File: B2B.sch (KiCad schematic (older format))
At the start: 3 parts, among them P4 CONN_01X14, P5 CONN_01X07, P6 CONN_01X07

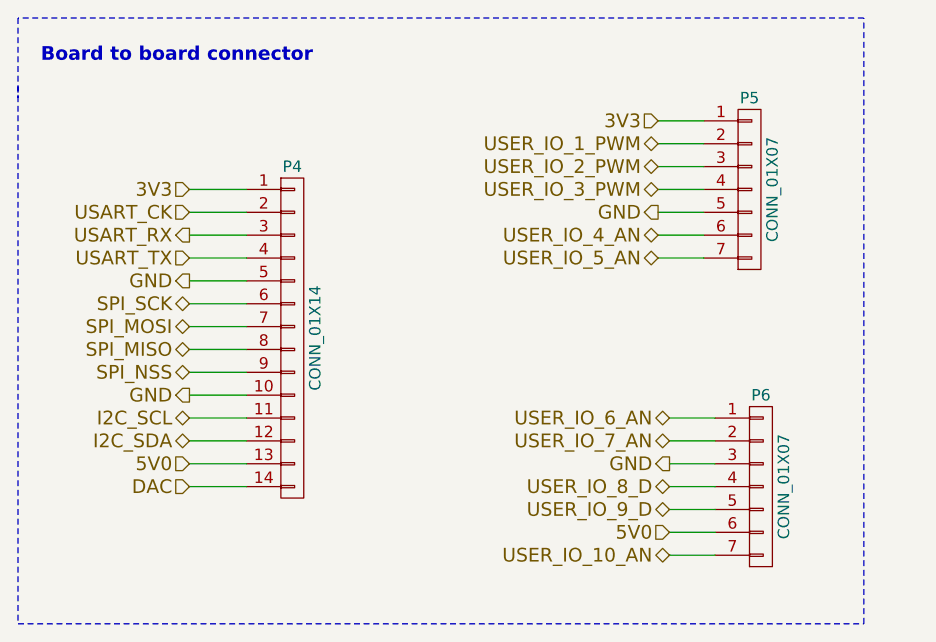
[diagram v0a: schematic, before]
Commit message: - #4 Added UART and CAN interface transceivers - Improved schematic structure - Removed all gerber outputs - Generated schematics outputs for PCB design - Updated local libraries
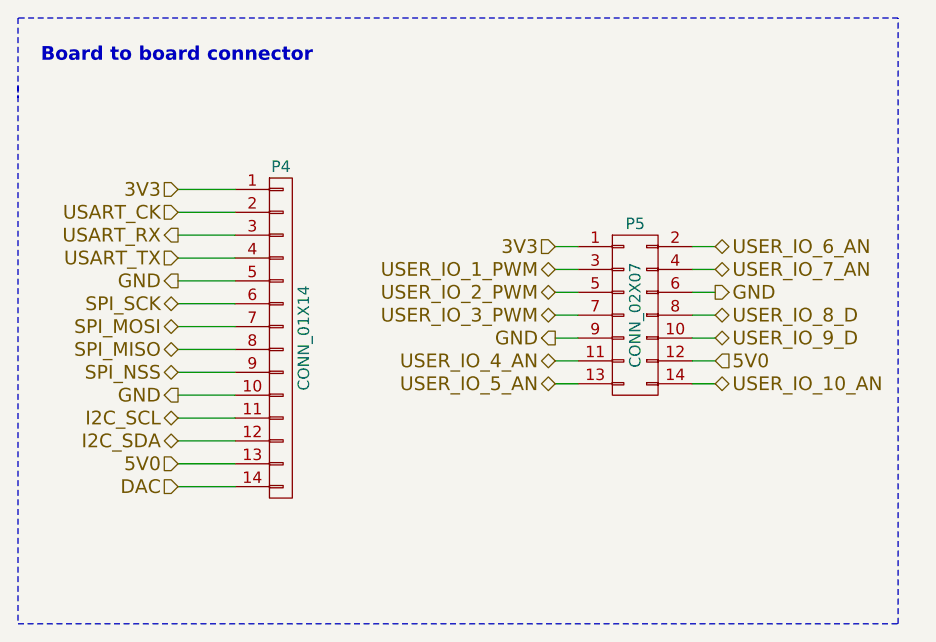
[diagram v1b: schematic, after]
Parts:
- removed P5, P6: CONN_01X07, symbol CONN_01X07
- added P5: CONN_02X07, Pin_Headers:Pin_Header_Straight_2x07, symbol CONN_02X07
- P4: footprint (none) -> Pin_Headers:Pin_Header_Straight_1x14
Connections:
- net 3V3: now also P5.1 (P1)
- net 5V0: now also P5.12 (P12)
- net GND: now also P5.6 (P6), P5.9 (P9)
- net USER_IO_10_AN: now also P5.14 (P14)
- net USER_IO_1_PWM: now also P5.3 (P3)
- net USER_IO_2_PWM: now also P5.5 (P5)
- net USER_IO_3_PWM: now also P5.7 (P7)
- net USER_IO_4_AN: now also P5.11 (P11)
- net USER_IO_5_AN: now also P5.13 (P13)
- net USER_IO_6_AN: now also P5.2 (P2)
- net USER_IO_7_AN: now also P5.4 (P4)
- net USER_IO_8_D: now also P5.8 (P8)
- net USER_IO_9_D: now also P5.10 (P10)
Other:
- moved on the sheet: P4
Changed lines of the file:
@@
 L CONN_01X14 P4
 U 1 1 56104092
-P 5350 4100
-F 0 "P4" H 5350 4850 50  0000 C CNN
-F 1 "CONN_01X14" V 5450 4100 50  0000 C CNN
-F 2 "" H 5350 4100 60  0000 C CNN
-F 3 "" H 5350 4100 60  0000 C CNN
-	1    5350 4100
+P 5300 4100
+F 0 "P4" H 5300 4850 50  0000 C CNN
+F 1 "CONN_01X14" V 5400 4100 50  0000 C CNN
+F 2 "Pin_Headers:Pin_Header_Straight_1x14" H 5300 4100 60  0001 C CNN
+F 3 "" H 5300 4100 60  0000 C CNN
+	1    5300 4100
 	1    0    0    -1
 $EndComp
-Text HLabel 4900 3450 0    60   Input ~ 0
+Text HLabel 4850 3450 0    60   Input ~ 0
 3V3
 Wire Wire Line
-	4900 3450 5150 3450
+	4850 3450 5100 3450
 Wire Wire Line
-	4900 3550 5150 3550
+	4850 3550 5100 3550
 Wire Wire Line
-	4900 3650 5150 3650
+	4850 3650 5100 3650
 Wire Wire Line
-	4900 3750 5150 3750
+	4850 3750 5100 3750
 Wire Wire Line
-	4900 3850 5150 3850
+	4850 3850 5100 3850
 Wire Wire Line
-	4900 3950 5150 3950
+	4850 3950 5100 3950
 Wire Wire Line
-	4900 4050 5150 4050
+	4850 4050 5100 4050
 Wire Wire Line
-	4900 4150 5150 4150
+	4850 4150 5100 4150
 Wire Wire Line
-	4900 4250 5150 4250
+	4850 4250 5100 4250
 Wire Wire Line
-	4900 4350 5150 4350
+	4850 4350 5100 4350
 Wire Wire Line
-	4900 4450 5150 4450
+	4850 4450 5100 4450
 Wire Wire Line
-	4900 4550 5150 4550
+	4850 4550 5100 4550
 Wire Wire Line
-	4900 4650 5150 4650
+	4850 4650 5100 4650
 Wire Wire Line
-	4900 4750 5150 4750
-Wire Wire Line
-	6950 3150 7150 3150
-Wire Wire Line
-	6950 3250 7150 3250
-Wire Wire Line
-	6950 3350 7150 3350
-Wire Wire Line
-	6950 3450 7150 3450
-Wire Wire Line
-	6950 3550 7150 3550
-Wire Wire Line
-	6950 3650 7150 3650
-Wire Wire Line
-	6950 3750 7150 3750
-Wire Wire Line
-	7000 4450 7200 4450
-Wire Wire Line
-	7000 4550 7200 4550
-Wire Wire Line
-	7000 4650 7200 4650
-Wire Wire Line
-	7000 4750 7200 4750
-Wire Wire Line
-	7000 4850 7200 4850
-Wire Wire Line
-	7000 4950 7200 4950
-Wire Wire Line
-	7000 5050 7200 5050
-Text HLabel 6950 3150 0    60   Input ~ 0
+	4850 4750 5100 4750
+Text HLabel 6500 3700 0    60   Input ~ 0
 3V3
-Text HLabel 6950 3550 0    60   Output ~ 0
+Text HLabel 6500 4100 0    60   Output ~ 0
 GND
-Text HLabel 7000 4650 0    60   Output ~ 0
+Text HLabel 7200 3900 2    60   Output ~ 0
 GND
-Text HLabel 4900 3850 0    60   Output ~ 0
+Text HLabel 4850 3850 0    60   Output ~ 0
 GND
-Text HLabel 4900 4350 0    60   Output ~ 0
+Text HLabel 4850 4350 0    60   Output ~ 0
 GND
-Text HLabel 7000 4950 0    60   Input ~ 0
+Text HLabel 7200 4200 2    60   Input ~ 0
 5V0
-Text HLabel 4900 4650 0    60   Input ~ 0
+Text HLabel 4850 4650 0    60   Input ~ 0
 5V0
-Text HLabel 4900 3550 0    60   Input ~ 0
+Text HLabel 4850 3550 0    60   Input ~ 0
 USART_CK
-Text HLabel 4900 3650 0    60   Output ~ 0
+Text HLabel 4850 3650 0    60   Output ~ 0
 USART_RX
-Text HLabel 4900 3750 0    60   Input ~ 0
+Text HLabel 4850 3750 0    60   Input ~ 0
 USART_TX
-Text HLabel 4900 3950 0    60   BiDi ~ 0
+Text HLabel 4850 3950 0    60   BiDi ~ 0
 SPI_SCK
-Text HLabel 4900 4050 0    60   BiDi ~ 0
+Text HLabel 4850 4050 0    60   BiDi ~ 0
 SPI_MOSI
-Text HLabel 4900 4150 0    60   BiDi ~ 0
+Text HLabel 4850 4150 0    60   BiDi ~ 0
 SPI_MISO
-Text HLabel 4900 4250 0    60   BiDi ~ 0
+Text HLabel 4850 4250 0    60   BiDi ~ 0
 SPI_NSS
-Text HLabel 4900 4450 0    60   BiDi ~ 0
+Text HLabel 4850 4450 0    60   BiDi ~ 0
 I2C_SCL
-Text HLabel 4900 4550 0    60   BiDi ~ 0
+Text HLabel 4850 4550 0    60   BiDi ~ 0
 I2C_SDA
-Text HLabel 4900 4750 0    60   Input ~ 0
+Text HLabel 4850 4750 0    60   Input ~ 0
 DAC
-Text HLabel 6950 3250 0    60   BiDi ~ 0
+Text HLabel 6500 3800 0    60   BiDi ~ 0
 USER_IO_1_PWM
-Text HLabel 6950 3350 0    60   BiDi ~ 0
+Text HLabel 6500 3900 0    60   BiDi ~ 0
 USER_IO_2_PWM
-Text HLabel 6950 3450 0    60   BiDi ~ 0
+Text HLabel 6500 4000 0    60   BiDi ~ 0
 USER_IO_3_PWM
-Text HLabel 6950 3650 0    60   BiDi ~ 0
+Text HLabel 6500 4200 0    60   BiDi ~ 0
 USER_IO_4_AN
-Text HLabel 6950 3750 0    60   BiDi ~ 0
+Text HLabel 6500 4300 0    60   BiDi ~ 0
 USER_IO_5_AN
-Text HLabel 7000 4450 0    60   BiDi ~ 0
+Text HLabel 7200 3700 2    60   BiDi ~ 0
 USER_IO_6_AN
-Text HLabel 7000 4550 0    60   BiDi ~ 0
+Text HLabel 7200 3800 2    60   BiDi ~ 0
 USER_IO_7_AN
-Text HLabel 7000 5050 0    60   BiDi ~ 0
+Text HLabel 7200 4300 2    60   BiDi ~ 0
 USER_IO_10_AN
-Text HLabel 7000 4750 0    60   BiDi ~ 0
+Text HLabel 7200 4000 2    60   BiDi ~ 0
 USER_IO_8_D
-Text HLabel 7000 4850 0    60   BiDi ~ 0
+Text HLabel 7200 4100 2    60   BiDi ~ 0
 USER_IO_9_D
-$Comp
-L CONN_01X07 P5
-U 1 1 5613F1BE
-P 7350 3450
-F 0 "P5" H 7350 3850 50  0000 C CNN
-F 1 "CONN_01X07" V 7450 3450 50  0000 C CNN
-F 2 "" H 7350 3450 60  0000 C CNN
-F 3 "" H 7350 3450 60  0000 C CNN
-	1    7350 3450
-	1    0    0    -1
-$EndComp
-$Comp
-L CONN_01X07 P6
-U 1 1 5613F1FA
-P 7400 4750
-F 0 "P6" H 7400 5150 50  0000 C CNN
-F 1 "CONN_01X07" V 7500 4750 50  0000 C CNN
-F 2 "" H 7400 4750 60  0000 C CNN
-F 3 "" H 7400 4750 60  0000 C CNN
-	1    7400 4750
-	1    0    0    -1
-$EndComp
 Wire Notes Line
 	4150 3000 4150 5350
 Wire Notes Line
-	4150 5350 7850 5350
+	4150 5350 8000 5350
 Wire Notes Line
-	7850 5350 7850 2700
+	8000 5350 8000 2700
 Wire Notes Line
-	7850 2700 4150 2700
+	8000 2700 4150 2700
 Wire Notes Line
 	4150 2700 4150 3050
 Text Notes 4250 2900 0    60   ~ 12
 Board to board connector
+$Comp
+L CONN_02X07 P5
+U 1 1 562CD45B
+P 6850 4000
+F 0 "P5" H 6850 4400 50  0000 C CNN
+F 1 "CONN_02X07" V 6850 4000 50  0000 C CNN
+F 2 "Pin_Headers:Pin_Header_Straight_2x07" H 6850 2800 60  0001 C CNN
+F 3 "" H 6850 2800 60  0000 C CNN
+	1    6850 4000
+	1    0    0    -1
+$EndComp
+Wire Wire Line
+	6500 3700 6600 3700
+Wire Wire Line
+	6500 3800 6600 3800
+Wire Wire Line
+	6500 3900 6600 3900
+Wire Wire Line
+	6500 4000 6600 4000
+Wire Wire Line
+	6500 4100 6600 4100
+Wire Wire Line
+	6500 4200 6600 4200
+Wire Wire Line
+	6500 4300 6600 4300
+Wire Wire Line
+	7100 3700 7200 3700
+Wire Wire Line
+	7100 3800 7200 3800
+Wire Wire Line
+	7100 3900 7200 3900
+Wire Wire Line
+	7100 4000 7200 4000
+Wire Wire Line
+	7100 4100 7200 4100
+Wire Wire Line
+	7200 4200 7100 4200
+Wire Wire Line
+	7200 4300 7100 4300
 $EndSCHEMATC
